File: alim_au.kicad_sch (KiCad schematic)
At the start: 13 parts, among them U6 TPS82130, U7 AMS1117-3.3

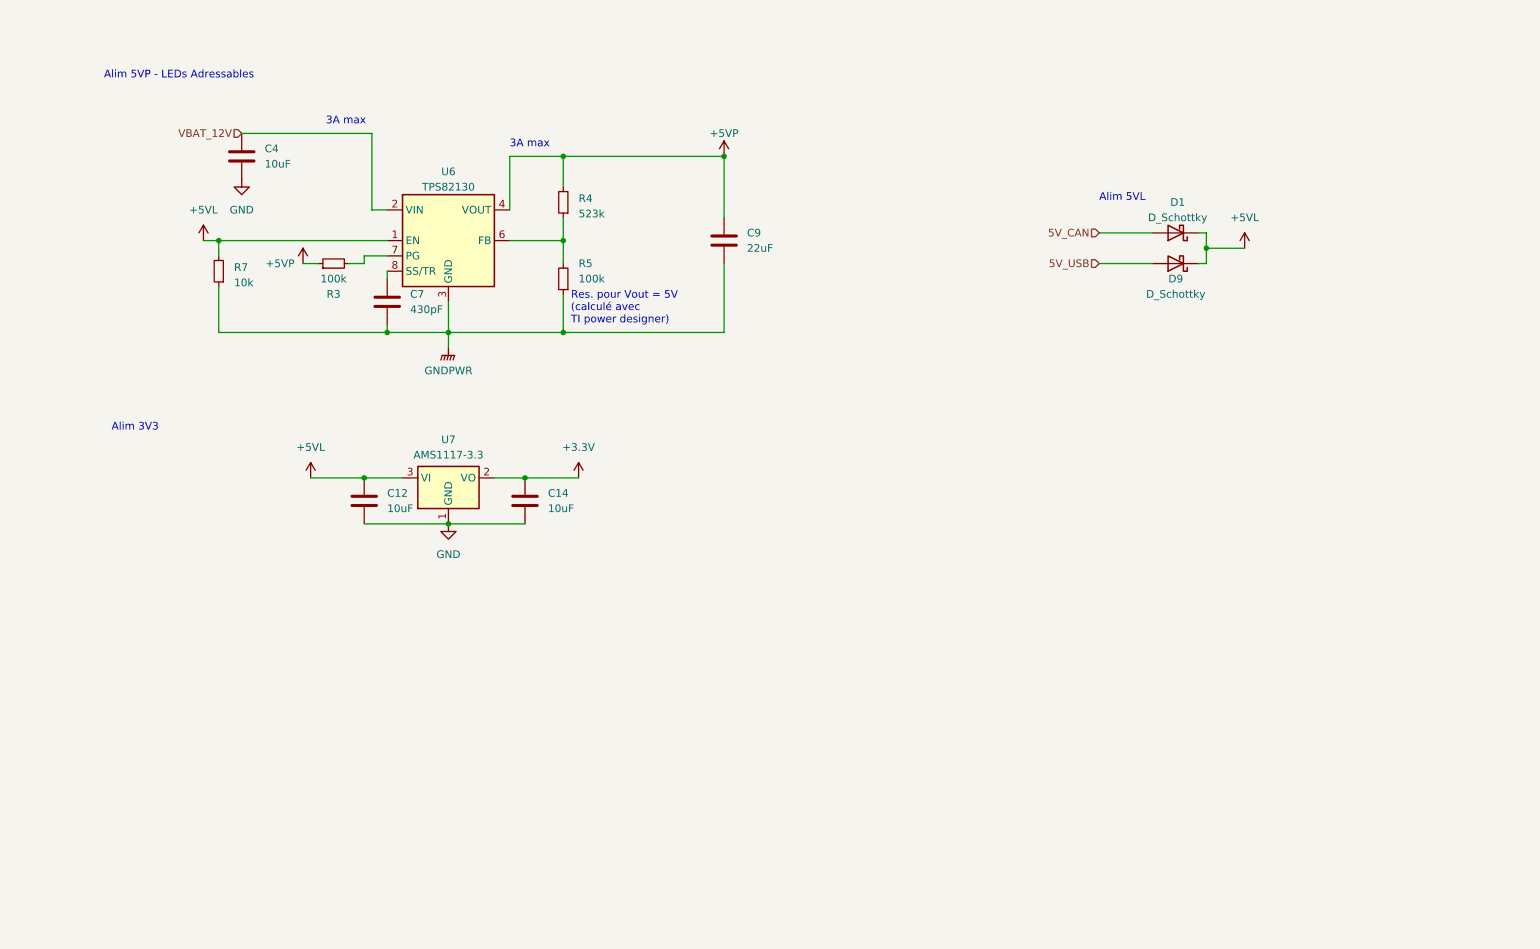
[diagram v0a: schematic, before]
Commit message: Simplification arborescence schema, correction duplicate designator TODO: connect floating signal on MCU sheet, update routing, split the board in two
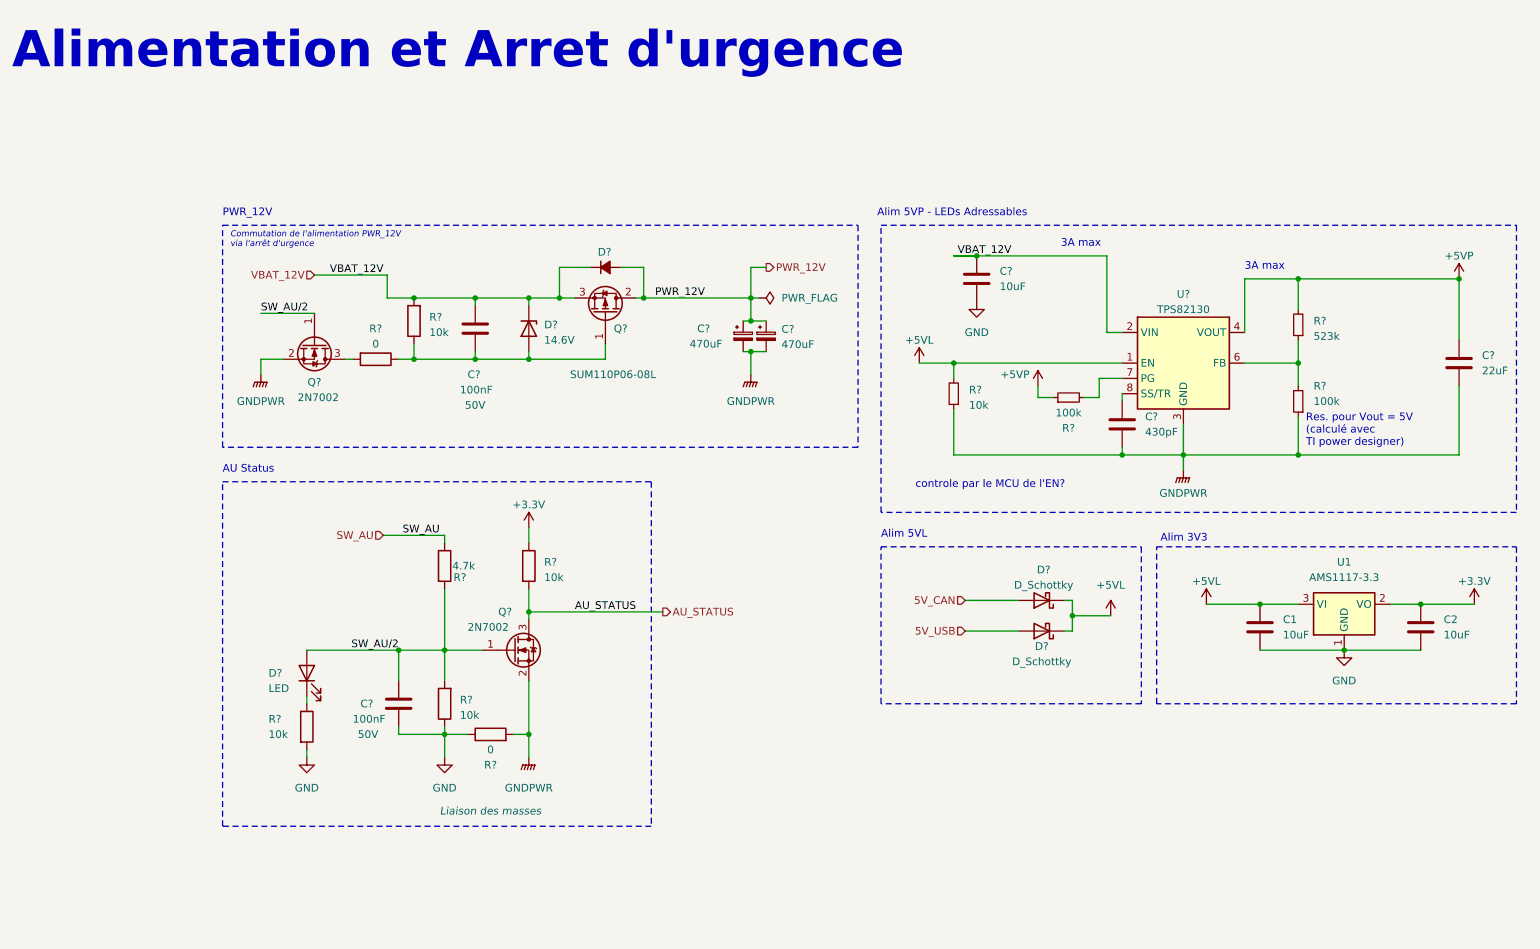
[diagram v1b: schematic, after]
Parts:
- removed C12, C14, C4: 10uF, Capacitor_SMD:C_0603_1608Metric, symbol Device:C
- removed C7: 430pF, Capacitor_SMD:C_0603_1608Metric, symbol Device:C
- removed C9: 22uF, Capacitor_SMD:C_0603_1608Metric, symbol Device:C
- removed D1, D9: D_Schottky, Diode_SMD:D_SOD-882, symbol Device:D_Schottky
- removed R3, R5: 100k, Resistor_SMD:R_0603_1608Metric, symbol Device:R_Small
- removed R4: 523k, Resistor_SMD:R_0603_1608Metric, symbol Device:R_Small
- removed R7: 10k, Resistor_SMD:R_0603_1608Metric, symbol Device:R_Small
- removed U6: TPS82130, Goldorak:MicroSiP, symbol Regulator_Switching:TPS82130
- removed U7: AMS1117-3.3, Package_TO_SOT_SMD:SOT-89-3, symbol Regulator_Linear:AMS1117-3.3
- added C1, C2, C?: 10uF, Capacitor_SMD:C_0603_1608Metric, symbol Device:C
- added C?: 22uF, Capacitor_SMD:C_0603_1608Metric, symbol Device:C
- added C? (x2): 100nF, Capacitor_SMD:C_0603_1608Metric, symbol Device:C
- added C? (x2): 470uF, Capacitor_THT:C_Radial_D8.0mm_H11.5mm_P3.50mm, symbol Device:C_Polarized_Small
- added C?: 430pF, Capacitor_SMD:C_0603_1608Metric, symbol Device:C
- added D? (x2): D_Schottky, Diode_SMD:D_SOD-882, symbol Device:D_Schottky
- added D?: ~, ComponentsEvo:DO-214AB, symbol Device:D_Small_Filled
- added D?: 14.6V, Diode_SMD:D_SOD-323, symbol Device:D_Zener
- added D?: LED, LED_SMD:LED_0603_1608Metric, symbol Device:LED
- added Q? (x2): 2N7002, Package_TO_SOT_SMD:SOT-23, symbol Transistor_FET:2N7002
- added Q?: SUM110P06-08L, Package_TO_SOT_SMD:TO-263-2, symbol Transistor_FET:QM6015D
- added R? (x4): 10k, Resistor_SMD:R_0603_1608Metric, symbol Device:R
- added R?: 0, Resistor_SMD:R_0603_1608Metric, symbol Device:R
- added R?: 0, Capacitor_SMD:C_0603_1608Metric, symbol Device:R
- added R?: 4.7k, Resistor_SMD:R_0603_1608Metric, symbol Device:R
- added R? (x2): 100k, Resistor_SMD:R_0603_1608Metric, symbol Device:R_Small
- added R?: 523k, Resistor_SMD:R_0603_1608Metric, symbol Device:R_Small
- added R?: 10k, Resistor_SMD:R_0603_1608Metric, symbol Device:R_Small
- added U1: AMS1117-3.3, Package_TO_SOT_SMD:SOT-89-3, symbol Regulator_Linear:AMS1117-3.3
- added U?: TPS82130, Goldorak:MicroSiP, symbol Regulator_Switching:TPS82130
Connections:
- net +3.3V: now also C2.1, R?.1, U1.2 (VO)
- net +5VL: now also C1.1, D?.1 (K), D?.1 (K), R?.2, U1.3 (VI), U?.1 (EN)
- net +5VP: now also C?.1, R?.1, R?.2, U?.4 (VOUT), U?.5 (VOUT)
- net 5V_CAN: now also D?.2 (A)
- net 5V_USB: now also D?.2 (A)
- net GND: now also C1.2, C2.2, C?.2, C?.2, R?.1, R?.1, R?.2, U1.1 (GND)
- net GNDPWR: now also C?.2, C?.2, C?.2, C?.2, Q?.2 (S), Q?.2 (S), R?.1, R?.1, R?.2, U?.3 (GND), U?.9 (GND)
- net VBAT_12V: now also C?.1, C?.1, D?.1 (K), D?.1 (K), Q?.3 (S), R?.2, U?.2 (VIN)
- new net: Q?.3 (D), R?.2
- new net: C?.2, D?.2 (A), Q?.1 (G), R?.1, R?.1
- new net: R?.1, R?.2, U?.6 (FB)
- new net: R?.2, U?.7 (PG)
- new net: C?.1, U?.8 (SS/TR)
- new net: D?.1 (K), R?.1
- new net AU_STATUS: Q?.3 (D), R?.2
- new net PWR_12V: C?.1, C?.1, D?.2 (A), Q?.2 (D)
- new net SW_AU: R?.1
- new net SW_AU/2: C?.1, D?.2 (A), Q?.1 (G), Q?.1 (G), R?.2, R?.2
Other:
- note added: "AU Status"
- note added: "Alimentation et Arret d'urgence"
- note added: "Commutation de l'alimentation PWR_12V via l'arrêt d'urgence"
- note added: "PWR_12V"
- note added: "controle par le MCU de l'EN?"
- company: (none) -> Équipe Goldorak
- title: (none) -> Carte pneumatique

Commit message: Correction de signaux non connectes, ajout de connecteur manquant, mise en forme du TOP
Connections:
- net 5V_CAN renamed 5L
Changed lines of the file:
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@@
 	)
 	(junction
+		(at 197.485 114.3)
+		(diameter 0)
+		(color 0 0 0 0)
+	)
+	(junction
 		(at 137.795 70.485)
 		(diameter 0)
@@
 		)
 		(stroke
-			(width 0)
+			(width 0.5)
 			(type default)
 			(color 0 0 0 1)
@@
 		)
 		(stroke
-			(width 1)
+			(width 0.5)
 			(type default)
 			(color 0 0 0 1)
@@
 		)
 		(stroke
-			(width 1)
+			(width 0.5)
 			(type default)
 			(color 255 0 0 1)
@@
 		)
 		(stroke
-			(width 0)
+			(width 0.5)
 			(type default)
+			(color 255 0 0 1)
 		)
 	)
@@
 		)
 		(stroke
-			(width 0)
+			(width 0.5)
 			(type default)
+			(color 255 0 0 1)
 		)
 	)
@@
 		)
 		(stroke
-			(width 0)
+			(width 0.5)
 			(type default)
+			(color 0 0 0 1)
 		)
 	)
@@
 		)
 		(stroke
-			(width 0)
+			(width 0.5)
 			(type default)
+			(color 255 0 0 1)
 		)
 	)
@@
 		)
 		(stroke
-			(width 1)
+			(width 0.5)
 			(type default)
 			(color 255 0 0 1)
@@
 			(width 0)
 			(type default)
-			(color 255 0 0 1)
 		)
 	)
@@
 		)
 		(stroke
-			(width 0)
+			(width 0.5)
 			(type default)
+			(color 255 0 0 1)
 		)
 	)
@@
 		)
 		(stroke
-			(width 1)
+			(width 0)
 			(type default)
-			(color 255 0 0 1)
 		)
 	)
@@
 		)
 		(stroke
-			(width 1)
+			(width 0.5)
 			(type default)
 			(color 0 0 0 1)
@@
 		)
 		(stroke
-			(width 0)
+			(width 0.5)
 			(type default)
+			(color 255 0 0 1)
 		)
 	)
@@
 		)
 		(stroke
-			(width 0)
+			(width 0.5)
 			(type default)
+			(color 0 0 0 1)
 		)
 	)
@@
 		)
 		(stroke
-			(width 0)
+			(width 0.5)
 			(type default)
+			(color 0 0 0 1)
 		)
 	)
@@
 		)
 		(stroke
-			(width 1)
+			(width 0.5)
 			(type default)
 			(color 0 0 0 1)
@@
 		)
 		(stroke
-			(width 0)
+			(width 0.5)
 			(type default)
+			(color 255 0 0 1)
 		)
 	)
@@
 		)
 		(stroke
-			(width 1)
+			(width 0)
 			(type default)
-			(color 255 0 13 1)
 		)
 	)
@@
 		)
 		(stroke
-			(width 0)
+			(width 0.5)
 			(type default)
+			(color 255 0 0 1)
 		)
 	)
@@
 			(width 0)
 			(type default)
-			(color 255 0 0 1)
 		)
 	)
@@
 		)
 		(stroke
-			(width 1)
+			(width 0.5)
 			(type default)
 			(color 0 0 0 1)
@@
 		)
 		(stroke
-			(width 0)
+			(width 0.5)
 			(type default)
+			(color 0 0 0 1)
 		)
 	)
@@
 		)
 		(stroke
-			(width 0)
+			(width 0.5)
 			(type default)
 			(color 0 0 0 1)
@@
 	(wire
 		(pts
-			(xy 248.92 112.395) (xy 257.81 112.395)
+			(xy 248.92 112.395) (xy 259.08 112.395)
 		)
 		(stroke
@@
 		)
 		(stroke
-			(width 0)
+			(width 0.5)
 			(type default)
 			(color 0 0 0 1)
@@
 		)
 		(stroke
-			(width 1)
+			(width 0)
 			(type default)
-			(color 255 0 6 1)
 		)
 	)
@@
 		)
 		(stroke
-			(width 0)
+			(width 0.5)
 			(type default)
 			(color 0 0 0 1)
@@
 		)
 		(stroke
-			(width 0)
+			(width 0.5)
 			(type default)
+			(color 0 0 0 1)
 		)
 	)
@@
 		)
 		(stroke
-			(width 0)
+			(width 0.5)
 			(type default)
+			(color 0 0 0 1)
 		)
 	)
@@
 		)
 		(stroke
-			(width 0)
+			(width 0.5)
 			(type default)
+			(color 0 0 0 1)
 		)
 	)
@@
 		)
 		(stroke
-			(width 0)
+			(width 0.5)
 			(type default)
+			(color 255 0 0 1)
 		)
 	)
@@
 		)
 		(stroke
-			(width 0)
+			(width 0.5)
 			(type default)
+			(color 255 0 0 1)
 		)
 	)
@@
 		)
 		(stroke
-			(width 1)
+			(width 0.5)
 			(type default)
 			(color 255 0 0 1)
@@
 		)
 		(stroke
-			(width 0)
+			(width 0.5)
 			(type default)
+			(color 0 0 0 1)
 		)
 	)
@@
 		)
 		(stroke
-			(width 0)
+			(width 0.5)
 			(type default)
 			(color 0 0 0 1)
@@
 		)
 		(stroke
-			(width 1)
+			(width 0.5)
 			(type default)
 			(color 255 0 0 1)
@@
 		)
 	)
-	(hierarchical_label "5V_CAN"
+	(hierarchical_label "5L"
 		(shape input)
 		(at 173.355 111.76 180)
@@
 	(symbol
 		(lib_id "power:+3.3V")
-		(at 257.81 112.395 0)
+		(at 259.08 112.395 0)
 		(unit 1)
 		(exclude_from_sim no)
@@
 		(dnp no)
 		(property "Reference" "#PWR3"
-			(at 257.81 116.205 0)
+			(at 259.08 116.205 0)
 			(effects
 				(font
@@
 		)
 		(property "Value" "+3.3V"
-			(at 257.81 108.585 0)
+			(at 259.08 108.585 0)
 			(effects
 				(font
@@
 		)
 		(property "Footprint" ""
-			(at 257.81 112.395 0)
+			(at 259.08 112.395 0)
 			(effects
 				(font
@@
 		)
 		(property "Datasheet" ""
-			(at 257.81 112.395 0)
+			(at 259.08 112.395 0)
 			(effects
 				(font
@@
 		)
 		(property "Description" ""
-			(at 257.81 112.395 0)
+			(at 259.08 112.395 0)
 			(effects
 				(font
@@
 					(unit 1)
 				)
+			)
+		)
+	)
+	(symbol
+		(lib_id "power:PWR_FLAG")
+		(at 197.485 114.3 180)
+		(unit 1)
+		(exclude_from_sim no)
+		(in_bom yes)
+		(on_board yes)
+		(dnp no)
+		(property "Reference" "#FLG5"
+			(at 197.485 116.205 0)
+			(effects
+				(font
+					(size 1.27 1.27)
+				)
+				(hide yes)
+			)
+		)
+		(property "Value" "PWR_FLAG"
+			(at 197.485 117.475 90)
+			(effects
+				(font
+					(size 1.27 1.27)
+				)
+				(justify left)
+			)
+		)
+		(property "Footprint" ""
+			(at 197.485 114.3 0)
+			(effects
+				(font
+					(size 1.27 1.27)
+				)
+				(hide yes)
+			)
+		)
+		(property "Datasheet" "~"
+			(at 197.485 114.3 0)
+			(effects
+				(font
+					(size 1.27 1.27)
+				)
+				(hide yes)
+			)
+		)
+		(property "Description" ""
+			(at 197.485 114.3 0)
+			(effects
+				(font
+					(size 1.27 1.27)
+				)
+				(hide yes)
+			)
+		)
+		(pin "1"
+		)
+		(instances
+			(project "12v-actuators-pcb"
+				(path "/d0b6cc72-ff07-4f5e-a148-04b65c86a715/a9998e65-7bac-4337-98c8-7de7c845405f"
+					(reference "#FLG5")
+					(unit 1)
+				)

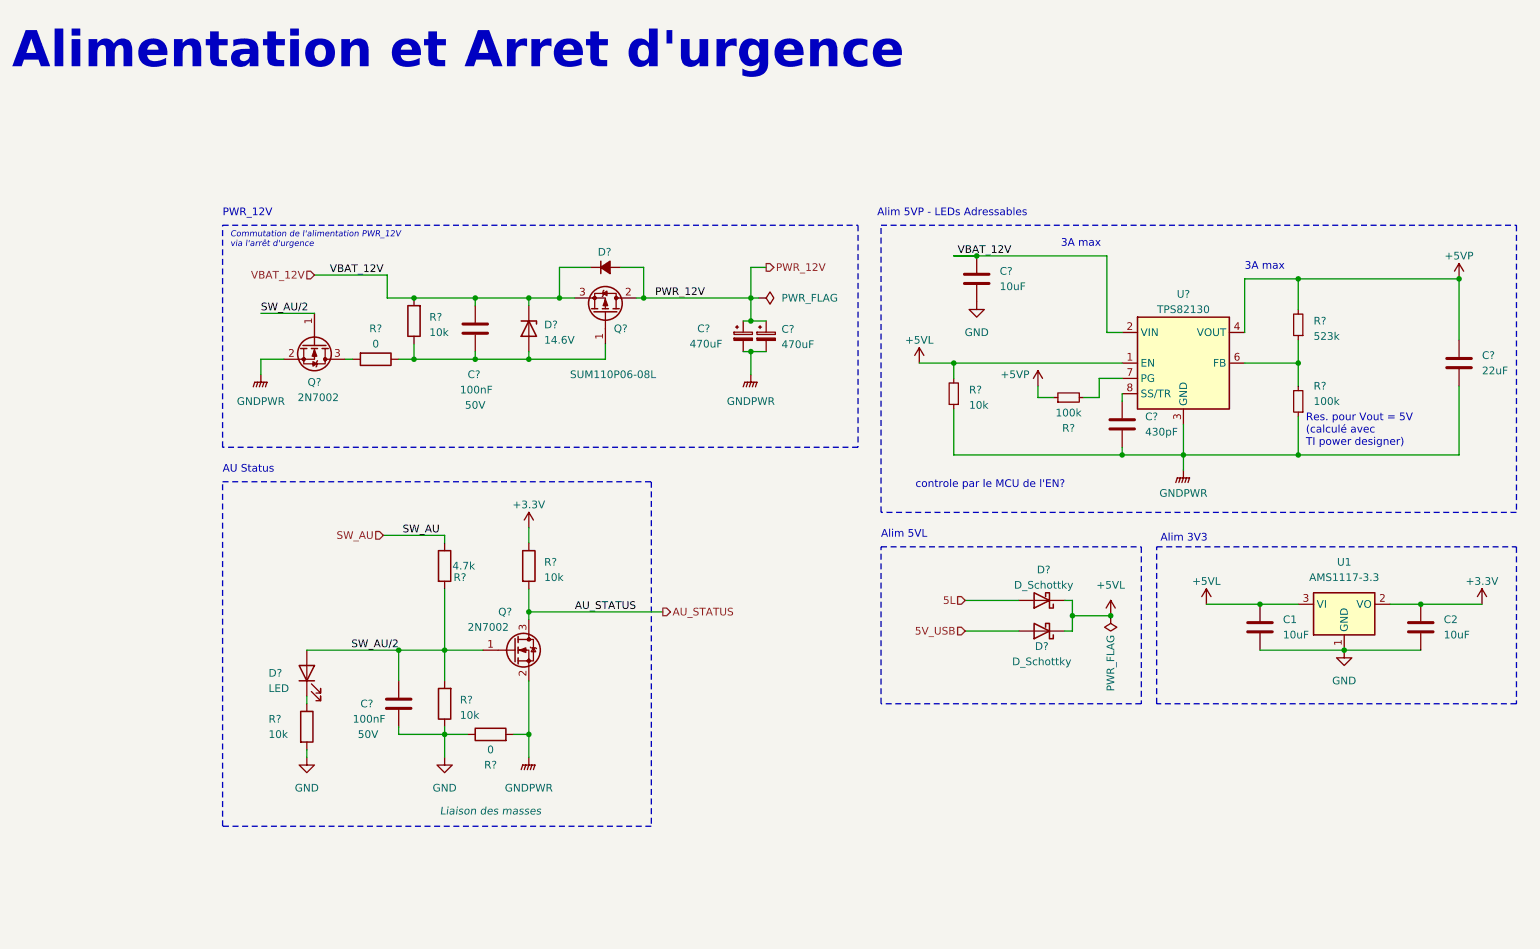
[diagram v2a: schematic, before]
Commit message: split des cartes
Todo: sync routage et ajout trou de fixation
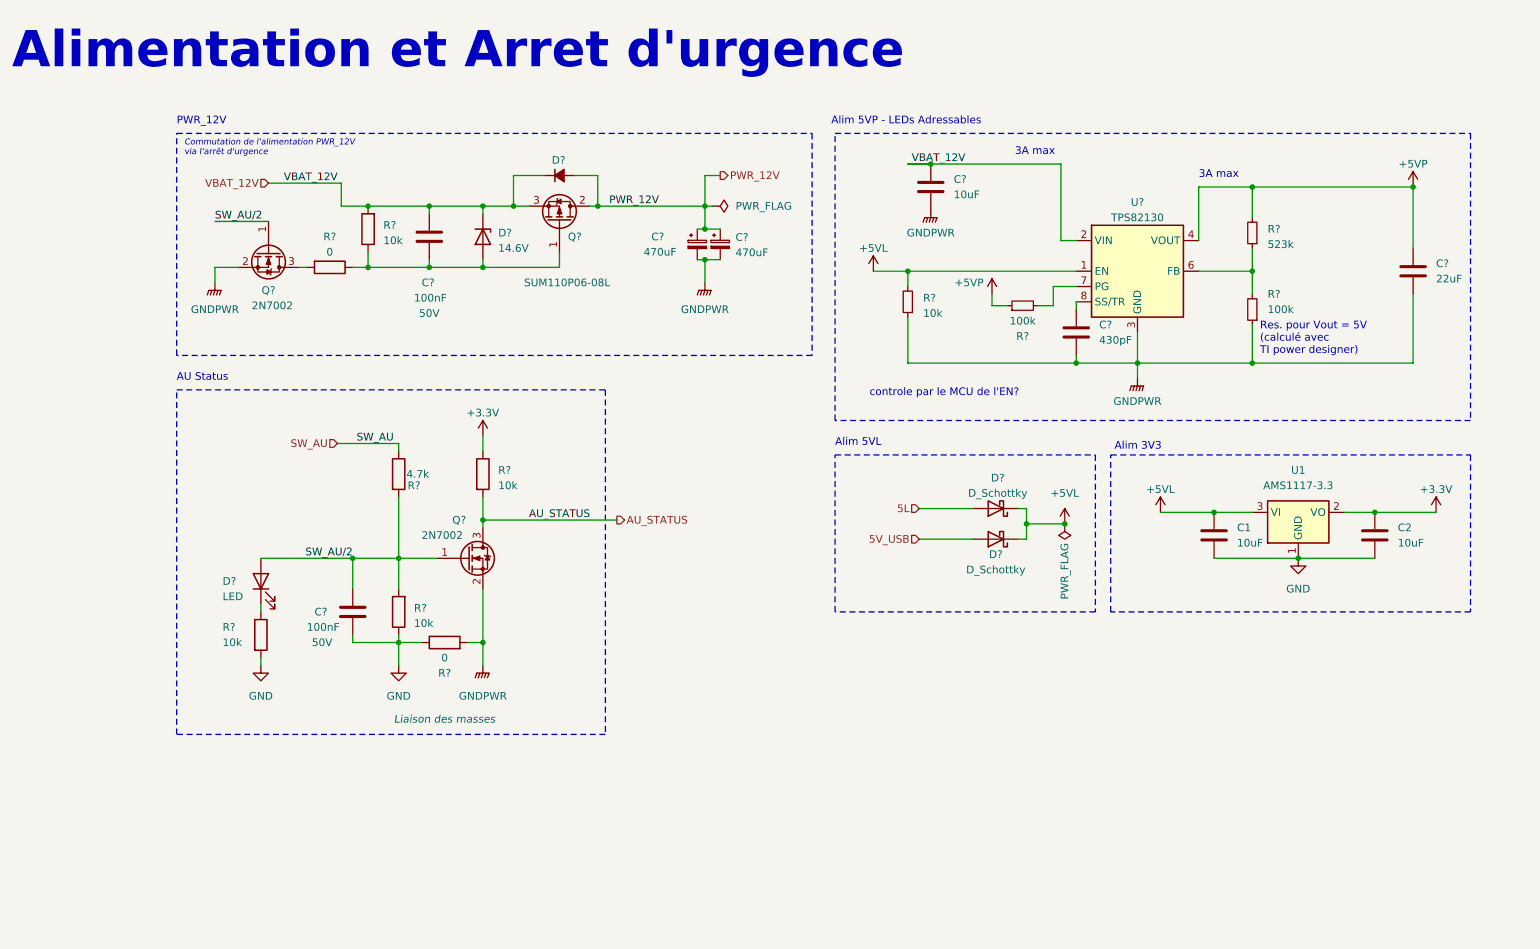
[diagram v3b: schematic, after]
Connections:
- net GND: no longer C?.2
- net GNDPWR: now also C?.2
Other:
- moved on the sheet: C1, C2, C?, D?, Q?, R?, U1, U?

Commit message: ajout d'une lib projet et synchro PCB
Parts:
- U?: footprint Goldorak:MicroSiP -> 12V-actuators_pcb:MicroSiP
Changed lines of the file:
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@@
 			)
 		)
-		(property "Footprint" "Goldorak:MicroSiP"
+		(property "Footprint" "12V-actuators_pcb:MicroSiP"
 			(at 201.93 73.66 0)
 			(effects
